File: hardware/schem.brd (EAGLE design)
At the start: 37.8 x 31.1 mm, 6 parts, among them IC1 7805L, IC2 TLE5205-2, U2 TINY85-20-DIP

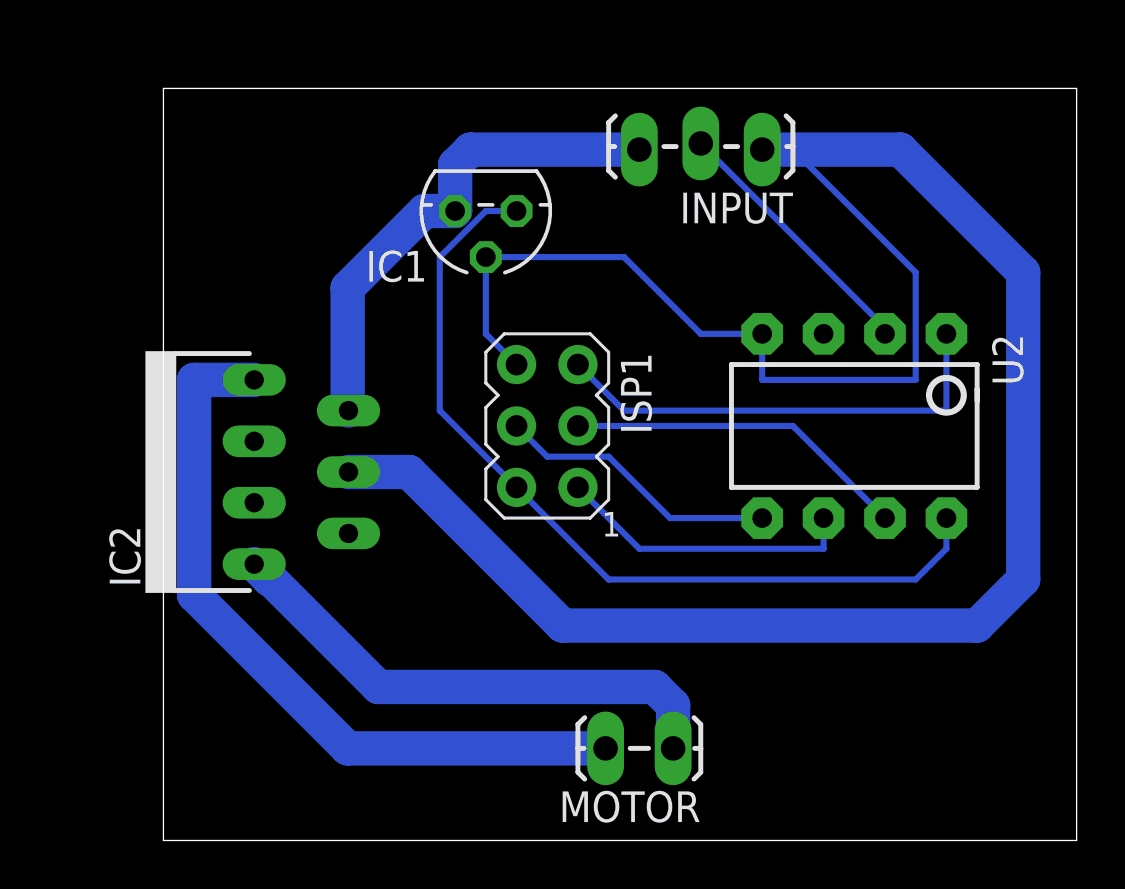
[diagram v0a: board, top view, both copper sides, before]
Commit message: changed pin inputs and re-rounted
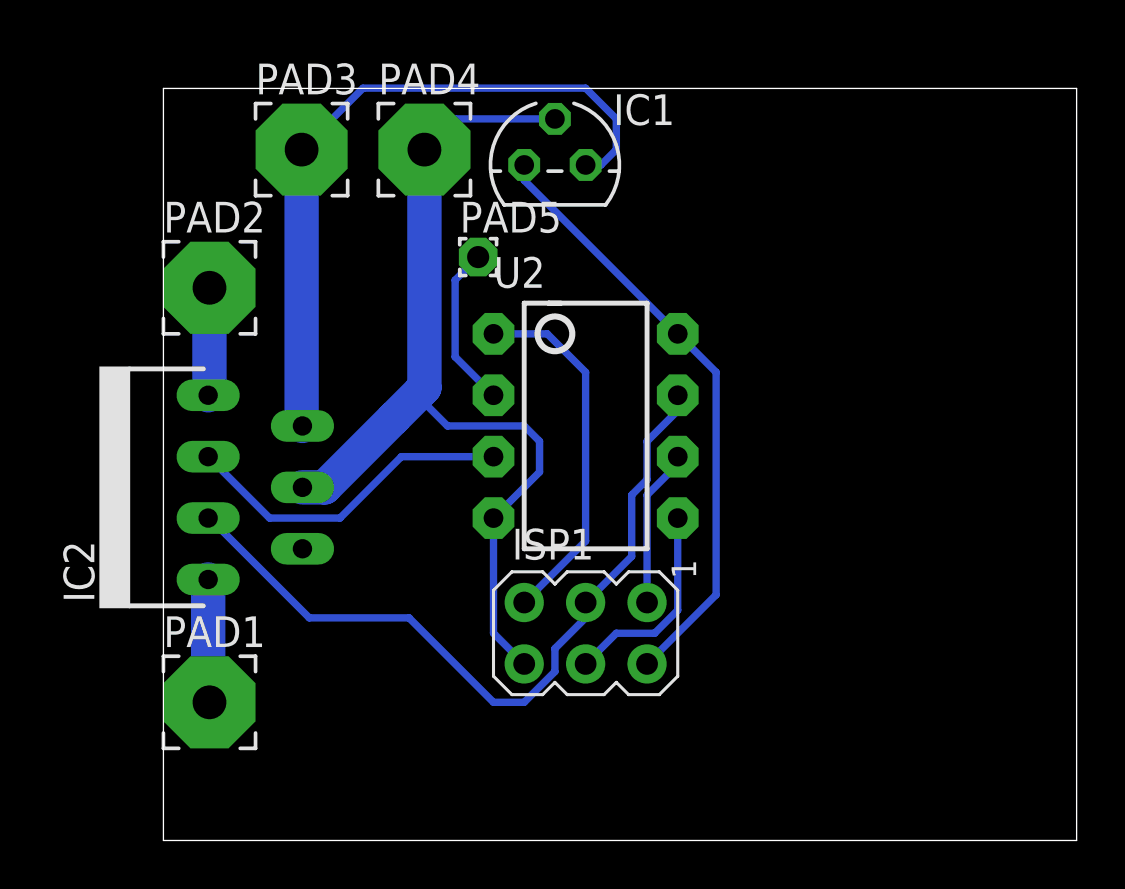
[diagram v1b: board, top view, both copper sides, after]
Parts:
- removed INPUT: (no value), SparkFun-Connectors:1X03_LOCK_LONGPADS
- removed MOTOR: M02LOCK_LONGPADS, SparkFun-Connectors:1X02_LOCK_LONGPADS
- added PAD1, PAD2, PAD3, PAD4: (no value), wirepad:3,81/1,4
- added PAD5: (no value), wirepad:1,6/0,9
- moved U2 11.1 mm to (33.3, 61.0), turned to 270 degrees
- moved ISP1 8.72 mm to (33.3, 52.4), turned to 270 degrees
- moved IC1 3.43 mm to (32.1, 71.8), turned to 0 degrees
- moved IC2 2.01 mm to (15.9, 58.4)
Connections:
- net +12V: now also PAD3.1; no longer INPUT.3
- net GND: now also PAD4.1; no longer INPUT.1
- net INP: now also PAD5.1; no longer INPUT.2
- net N$1: now also PAD1.1; no longer MOTOR.1
- net N$4: now also PAD2.1; no longer MOTOR.2
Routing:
- net GND: track 95.8 -> 39.5 mm
- net N$4: track 31.0 -> 4.47 mm
- net SCK: track 14.3 -> 31.6 mm
- net N$1: track 21.5 -> 5.10 mm
- net N$2: track 0.00 -> 13.9 mm
- net +5V: track 36.0 -> 25.1 mm
- net +12V: track 20.6 -> 28.8 mm
- net MISO: track 12.5 -> 6.56 mm
- net INP: track 11.0 -> 6.77 mm
- net RST: track 19.2 -> 15.0 mm
- net MOSI: track 11.7 -> 8.54 mm

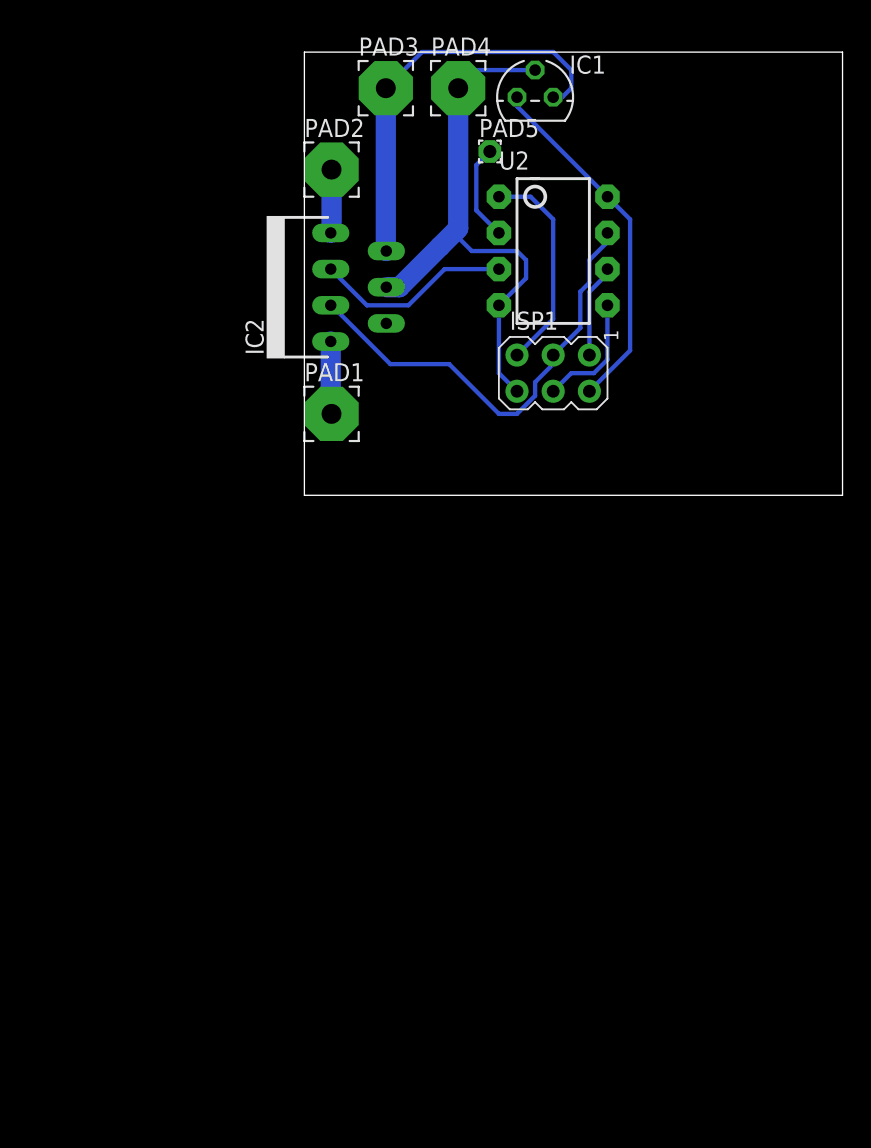
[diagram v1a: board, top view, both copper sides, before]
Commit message: compated board size
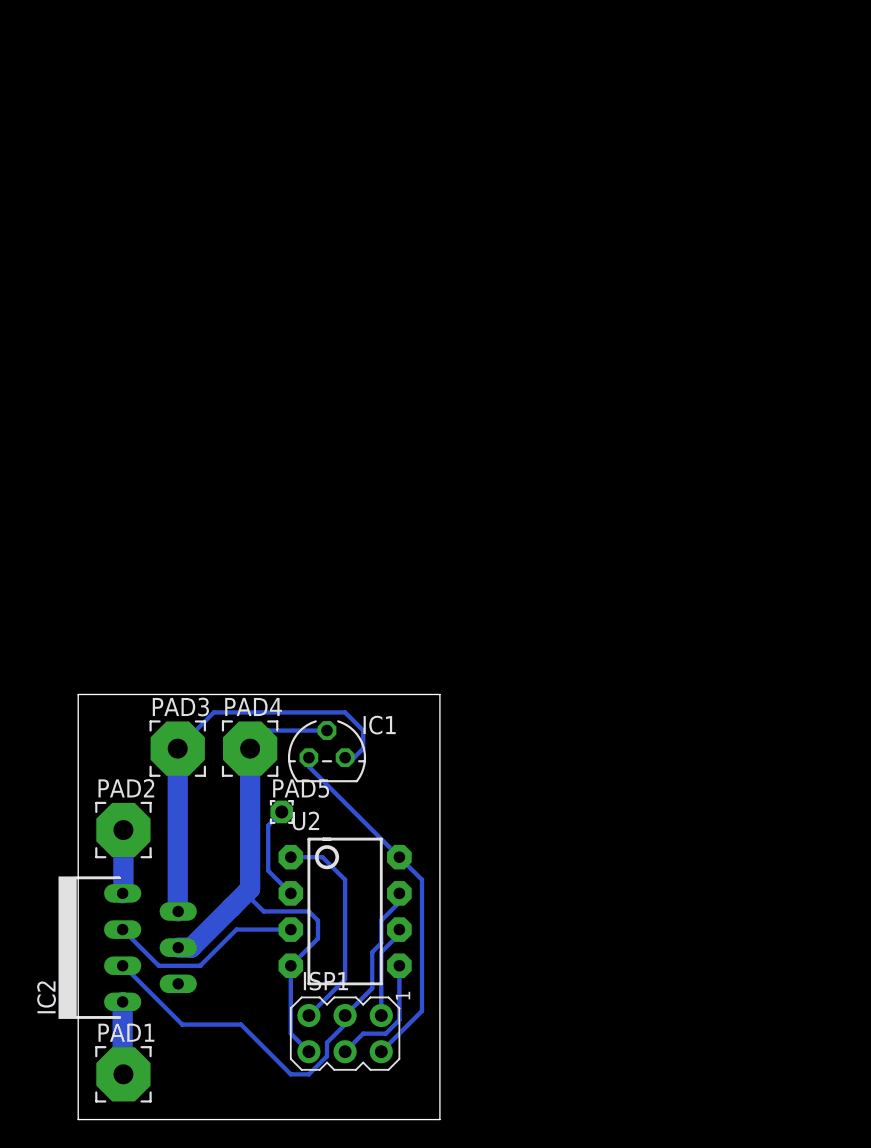
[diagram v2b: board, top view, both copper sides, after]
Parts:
- moved IC2 48.6 mm to (1.27, 12.1)
- moved ISP1 48.6 mm to (18.7, 6.03)
- moved PAD1 48.6 mm to (3.17, 3.17)
- moved PAD3 48.6 mm to (6.99, 26.0)
- moved PAD4 48.6 mm to (12.1, 26.0)
- moved U2 48.6 mm to (18.7, 14.6)
- moved IC1 48.6 mm to (17.5, 25.4)
- moved PAD2 48.6 mm to (3.17, 20.3)
- moved PAD5 48.6 mm to (14.3, 21.6)
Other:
- board size 37.8 x 31.1 mm -> 25.4 x 29.8 mm

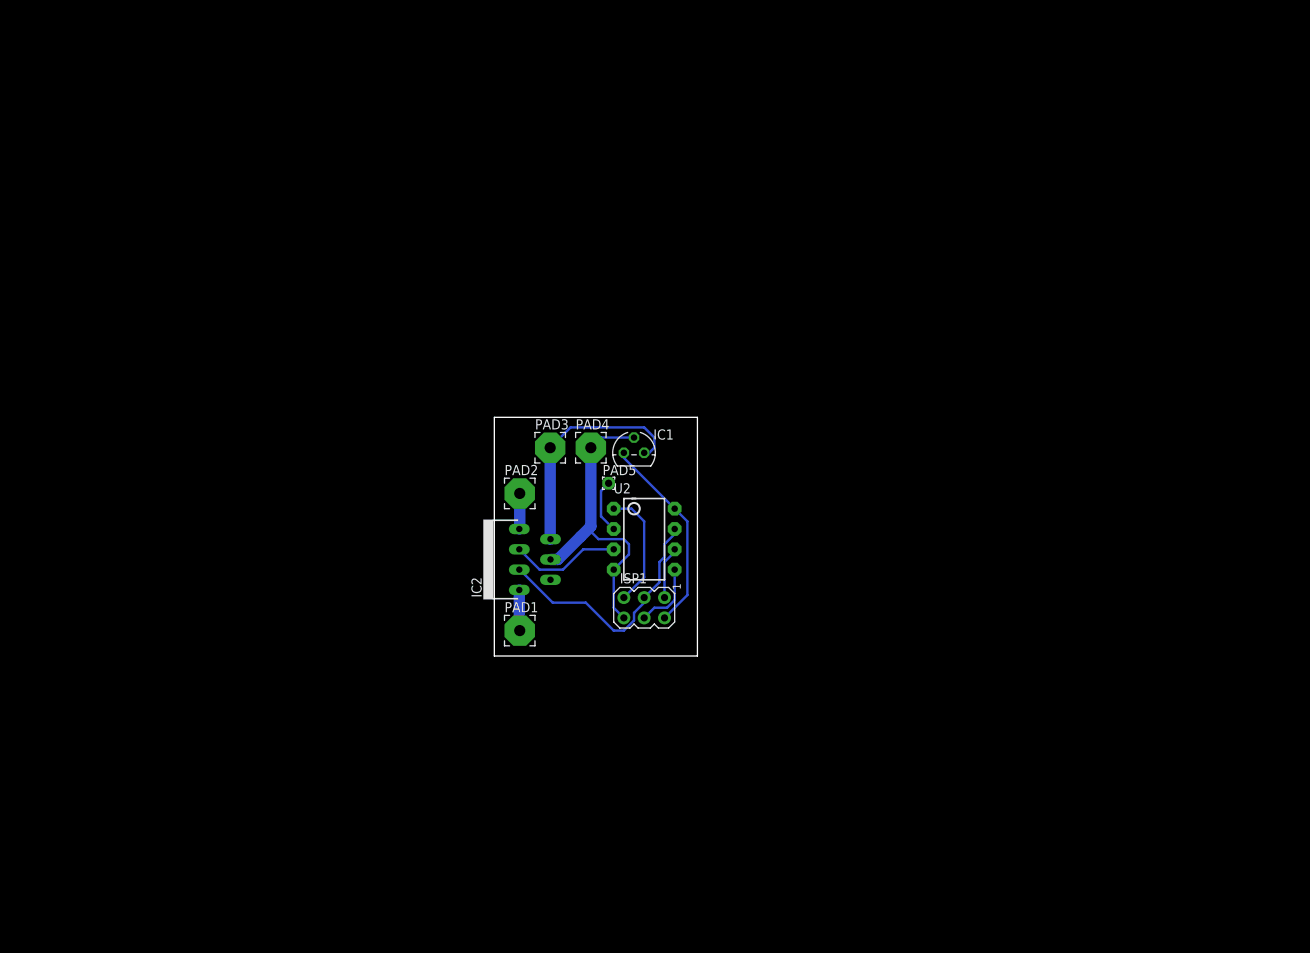
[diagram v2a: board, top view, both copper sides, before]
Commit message: Updated Schematic
Used new IC H Bridge and cleaned up schematic
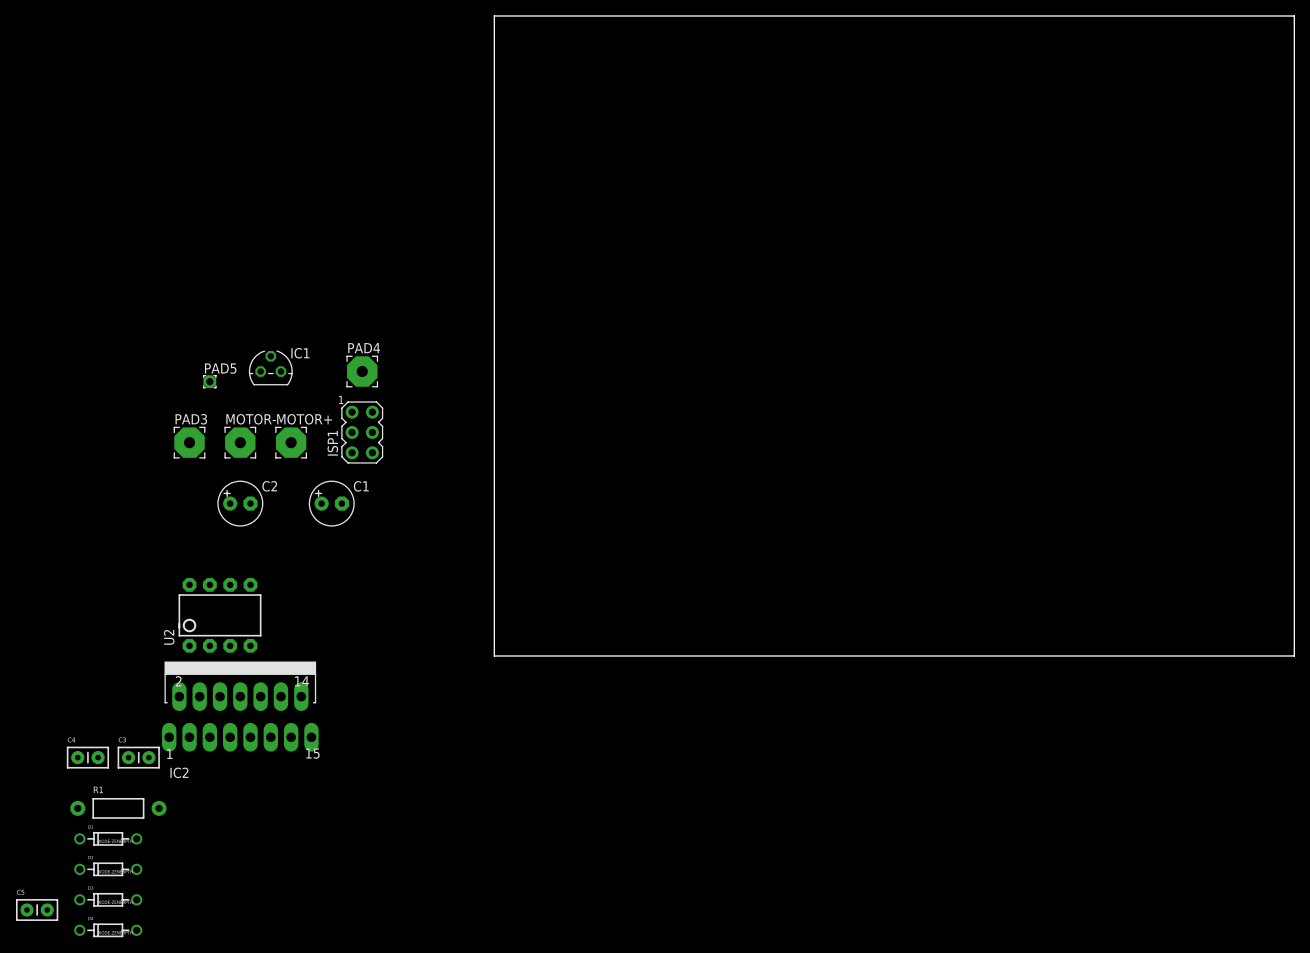
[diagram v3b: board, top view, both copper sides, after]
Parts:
- removed PAD1, PAD2: (no value), wirepad:3,81/1,4
- added C1, C2: (no value), adafruit:E2,5-6
- added C3, C4, C5: 100nF, SparkFun-Capacitors:CAP-PTH-SMALL2
- added D1, D2, D3, D4: DIODE-ZENERPTH, SparkFun-DiscreteSemi:DIODE-ZENER
- added MOTOR+, MOTOR-: (no value), wirepad:3,81/1,4
- added R1: (no value), SparkFun-Passives:AXIAL-0.4
- IC2: value TLE5205-2 -> L298; device infineon:P-TO220-7-11 -> st-microelectronics:MULTIWATT-15
- moved U2 53.9 mm to (-34.3, 5.08), turned to 0 degrees
- moved PAD5 51.4 mm to (-35.6, 34.3)
- moved IC1 46.5 mm to (-27.9, 35.6)
- moved PAD3 45.1 mm to (-38.1, 26.7)
- moved ISP1 41.5 mm to (-16.5, 27.9), turned to 0 degrees
- moved IC2 36.1 mm to (-31.8, -2.54), turned to 0 degrees
- moved PAD4 30.1 mm to (-16.5, 35.6)
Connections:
- removed net N$2: IC2.5, U2.3
- removed net N$4: IC2.7, PAD2.1
- new net IN2: IC2.10, IC2.7, U2.3
- new net OUT1: D1.P$2, D2.P$1, IC2.14, IC2.2, MOTOR+.1
- new net OUT2: D3.P$2, D4.P$1, IC2.13, IC2.3, MOTOR-.1
- net +12V: now also C1.+, C4.1, C5.2, D1.P$1, D3.P$1, IC2.4; no longer IC2.6
- net +5V: now also C2.+, C3.2, IC2.9
- net GND: now also C1.-, C2.-, C3.1, C4.2, C5.1, D2.P$2, D4.P$2, IC2.8, R1.P$2; no longer IC2.4
- net MISO: now also IC2.11, IC2.6
- net N$1: now also IC2.15, R1.P$1; no longer PAD1.1
- net SCK: now also IC2.12, IC2.5; no longer IC2.3
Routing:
- net GND: track 39.5 -> 0.00 mm
- net SCK: track 31.6 -> 0.00 mm
- net +12V: track 28.8 -> 0.00 mm
- net +5V: track 25.1 -> 0.00 mm
- net RST: track 15.0 -> 0.00 mm
- net N$2: track 13.9 -> 0.00 mm
- net MOSI: track 8.54 -> 0.00 mm
- net INP: track 6.77 -> 0.00 mm
- net MISO: track 6.56 -> 0.00 mm
- net N$1: track 5.10 -> 0.00 mm
- net N$4: track 4.47 -> 0.00 mm
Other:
- board size 25.4 x 29.8 mm -> 100 x 80 mm

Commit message: Routed board
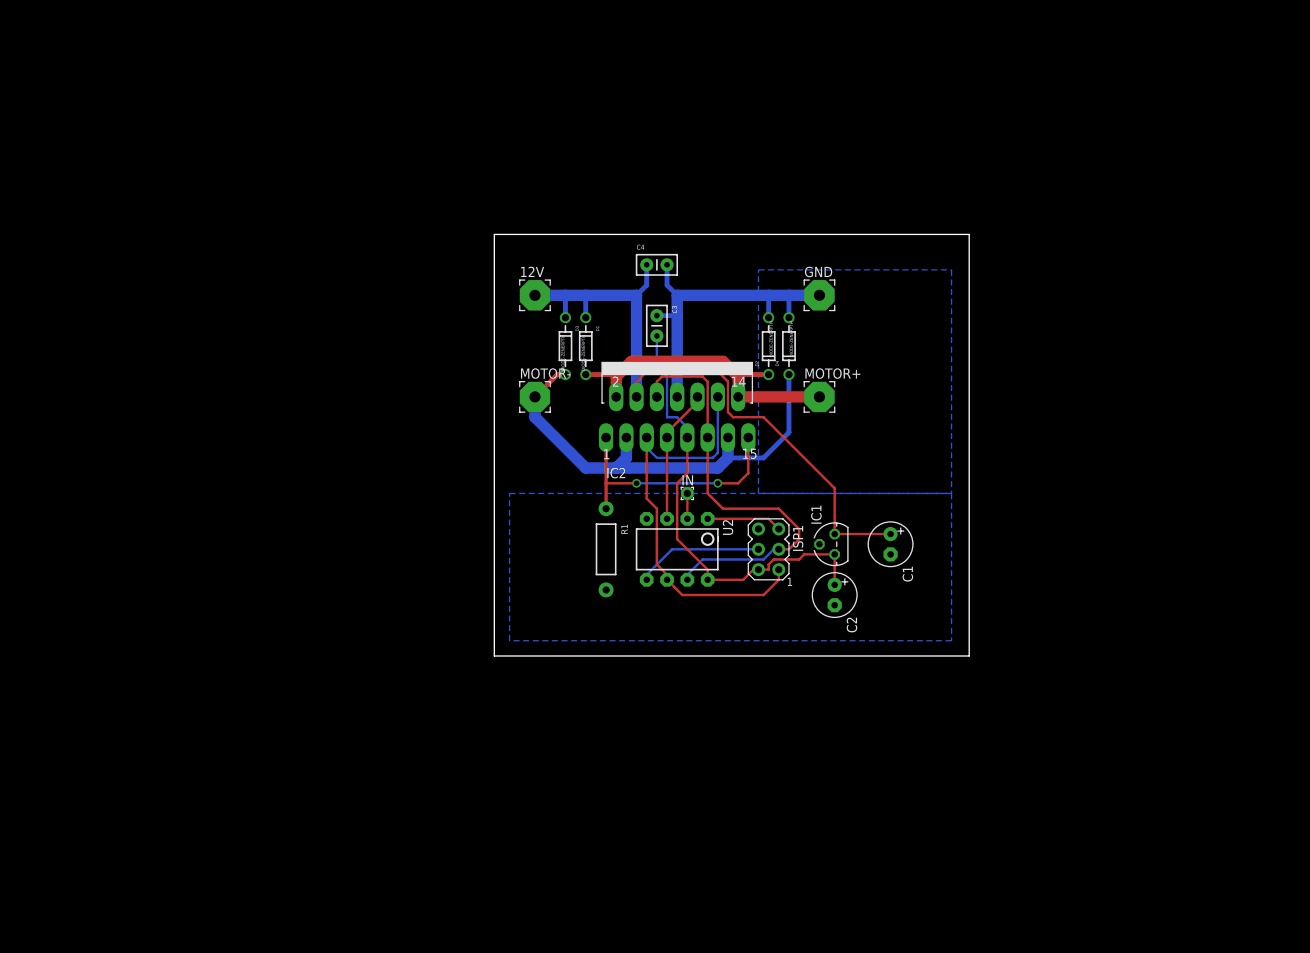
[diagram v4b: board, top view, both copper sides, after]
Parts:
- removed C5: 100nF, SparkFun-Capacitors:CAP-PTH-SMALL2
- removed PAD3, PAD4: (no value), wirepad:3,81/1,4
- removed PAD5: (no value), wirepad:1,6/0,9
- added 12V, GND: (no value), wirepad:3,81/1,4
- added IN: (no value), wirepad:1,6/0,9
- moved D4 112.1 mm to (36.8, 38.7), turned to 90 degrees
- moved D2 105.3 mm to (34.3, 38.7), turned to 90 degrees
- moved C4 94.1 mm to (19.1, 48.9)
- moved D3 89.8 mm to (8.89, 38.7), turned to 270 degrees
- moved C3 86.1 mm to (20.3, 42.5), turned to 270 degrees
- moved D1 85.8 mm to (11.4, 38.7), turned to 270 degrees
- moved C2 75.2 mm to (42.5, 7.62), turned to 270 degrees
- moved IC1 73.7 mm to (42.5, 14.0), turned to 90 degrees
- moved C1 70.0 mm to (49.5, 14.0), turned to 270 degrees
- moved R1 69.0 mm to (14.0, 13.3), turned to 270 degrees
- moved MOTOR+ 66.3 mm to (40.6, 32.4)
- moved IC2 66.2 mm to (22.9, 34.9)
- moved U2 57.7 mm to (22.9, 13.3), turned to 180 degrees
- moved ISP1 52.9 mm to (34.3, 13.3), turned to 180 degrees
- moved MOTOR- 37.3 mm to (5.08, 32.4)
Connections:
- net +12V: now also 12V.1; no longer C5.2, PAD3.1
- net GND: now also GND.1; no longer C5.1, PAD4.1
- net INP: now also IN.1; no longer PAD5.1
- net MISO: now also IC2.12, IC2.5; no longer IC2.11, IC2.6
- net SCK: now also IC2.11, IC2.6; no longer IC2.12, IC2.5
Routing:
- net +12V: track 0.00 -> 83.5 mm
- net GND: track 0.00 -> 73.4 mm
- net OUT2: track 0.00 -> 57.8 mm
- net +5V: track 0.00 -> 56.3 mm
- net SCK: track 0.00 -> 53.7 mm
- net MISO: track 0.00 -> 53.6 mm
- net OUT1: track 0.00 -> 39.9 mm
- net N$1: track 0.00 -> 31.6 mm, vias 0 -> 2
- net IN2: track 0.00 -> 16.8 mm
- net MOSI: track 0.00 -> 15.9 mm
- net RST: track 0.00 -> 9.42 mm
- net INP: track 0.00 -> 3.18 mm
- added copper zone on layer 16, net GND
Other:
- board size 100 x 80 mm -> 59.4 x 52.7 mm
